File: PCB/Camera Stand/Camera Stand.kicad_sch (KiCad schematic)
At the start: 6 parts, among them J2 HMC5883L, J3 Motor Drive, J4 Keypad 4x4, J9 GPS Module, M5 Motor_Servo, U1 NRF24L01

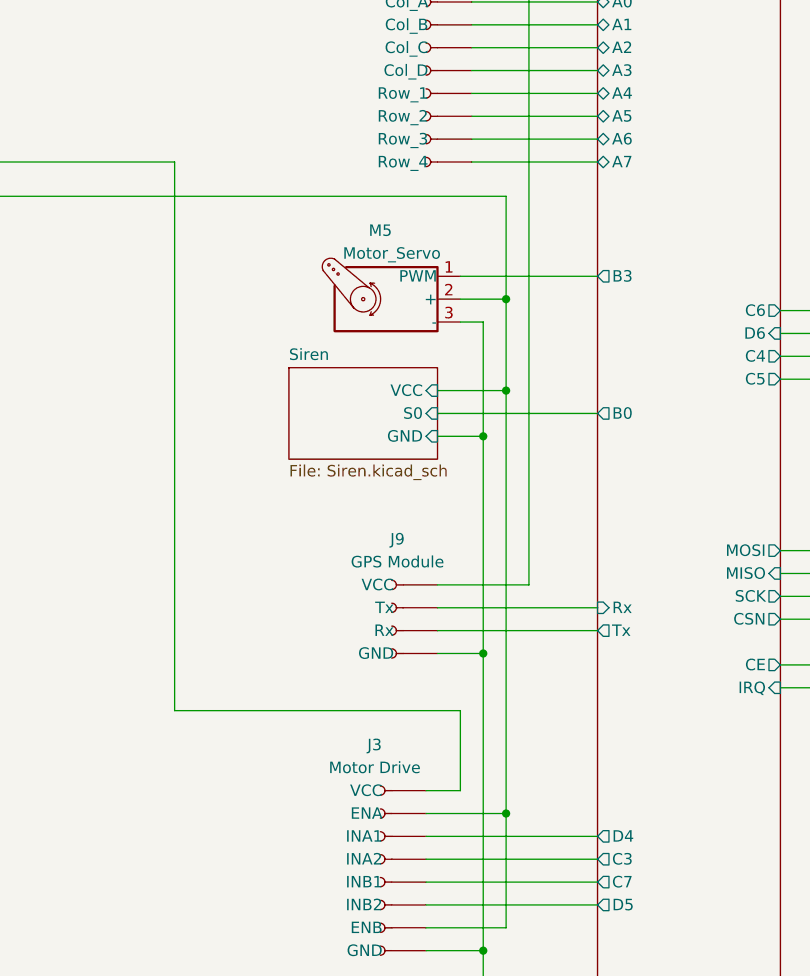
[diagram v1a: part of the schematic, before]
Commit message: 12v to siren
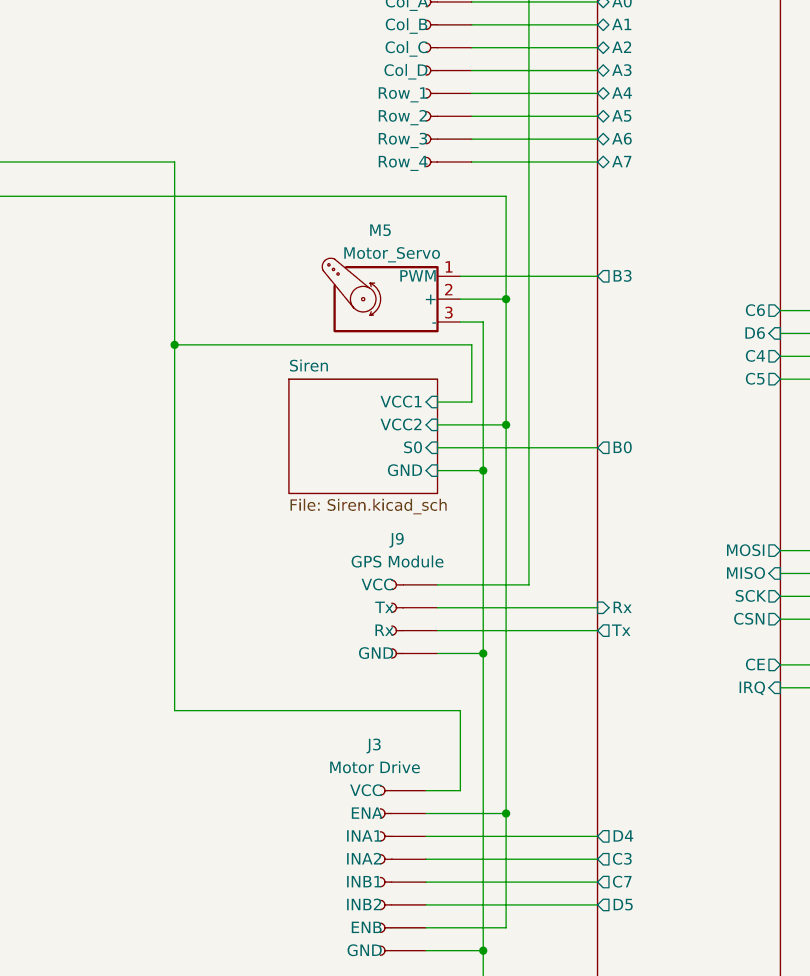
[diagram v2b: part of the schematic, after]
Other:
- sheet Siren ports: added VCC1, VCC2; removed VCC
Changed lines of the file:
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@@
 (kicad_sch (version 20211123) (generator eeschema)
   (paper "A4")
-  (junction (at 146.05 82.55) (diameter 0) (color 0 0 0 0)
-  )
   (junction (at 208.28 59.69) (diameter 0) (color 0 0 0 0)
   )
+  (junction (at 109.22 77.47) (diameter 0) (color 0 0 0 0)
+  )
   (junction (at 148.59 19.05) (diameter 0) (color 0 0 0 0)
   )
@@
   (junction (at 143.51 148.59) (diameter 0) (color 0 0 0 0)
   )
+  (junction (at 143.51 91.44) (diameter 0) (color 0 0 0 0)
+  )
+  (junction (at 146.05 86.36) (diameter 0) (color 0 0 0 0)
+  )
   (junction (at 210.82 29.21) (diameter 0) (color 0 0 0 0)
   )
@@
   (junction (at 146.05 72.39) (diameter 0) (color 0 0 0 0)
   )
-  (junction (at 143.51 87.63) (diameter 0) (color 0 0 0 0)
-  )
   (junction (at 87.63 60.96) (diameter 0) (color 0 0 0 0)
   )
@@
     (stroke (width 0) (type default) (color 0 0 0 0))
   )
+  (wire (pts (xy 138.43 83.82) (xy 142.24 83.82))
+    (stroke (width 0) (type default) (color 0 0 0 0))
+  )
   (wire (pts (xy 176.53 115.57) (xy 217.17 115.57))
     (stroke (width 0) (type default) (color 0 0 0 0))
@@
     (stroke (width 0) (type default) (color 0 0 0 0))
   )
-  (wire (pts (xy 138.43 85.09) (xy 156.21 85.09))
+  (wire (pts (xy 138.43 88.9) (xy 156.21 88.9))
     (stroke (width 0) (type default) (color 0 0 0 0))
   )
@@
     (stroke (width 0) (type default) (color 0 0 0 0))
   )
+  (wire (pts (xy 146.05 72.39) (xy 146.05 86.36))
+    (stroke (width 0) (type default) (color 0 0 0 0))
+  )
   (wire (pts (xy 218.44 71.12) (xy 210.82 71.12))
     (stroke (width 0) (type default) (color 0 0 0 0))
@@
     (stroke (width 0) (type default) (color 0 0 0 0))
   )
-  (wire (pts (xy 143.51 87.63) (xy 143.51 111.76))
-    (stroke (width 0) (type default) (color 0 0 0 0))
-  )
-  (wire (pts (xy 146.05 82.55) (xy 146.05 129.54))
-    (stroke (width 0) (type default) (color 0 0 0 0))
-  )
   (wire (pts (xy 176.53 78.74) (xy 218.44 78.74))
     (stroke (width 0) (type default) (color 0 0 0 0))
@@
     (stroke (width 0) (type default) (color 0 0 0 0))
   )
+  (wire (pts (xy 143.51 91.44) (xy 143.51 111.76))
+    (stroke (width 0) (type default) (color 0 0 0 0))
+  )
   (wire (pts (xy 87.63 148.59) (xy 87.63 156.21))
     (stroke (width 0) (type default) (color 0 0 0 0))
   )
+  (wire (pts (xy 146.05 86.36) (xy 146.05 129.54))
+    (stroke (width 0) (type default) (color 0 0 0 0))
+  )
   (wire (pts (xy 208.28 83.82) (xy 218.44 83.82))
     (stroke (width 0) (type default) (color 0 0 0 0))
@@
     (stroke (width 0) (type default) (color 0 0 0 0))
   )
-  (wire (pts (xy 143.51 74.93) (xy 143.51 87.63))
-    (stroke (width 0) (type default) (color 0 0 0 0))
-  )
   (wire (pts (xy 76.2 60.96) (xy 87.63 60.96))
     (stroke (width 0) (type default) (color 0 0 0 0))
@@
     (stroke (width 0) (type default) (color 0 0 0 0))
   )
-  (wire (pts (xy 146.05 72.39) (xy 146.05 82.55))
-    (stroke (width 0) (type default) (color 0 0 0 0))
-  )
   (wire (pts (xy 143.51 148.59) (xy 156.21 148.59))
     (stroke (width 0) (type default) (color 0 0 0 0))
@@
     (stroke (width 0) (type default) (color 0 0 0 0))
   )
+  (wire (pts (xy 109.22 77.47) (xy 142.24 77.47))
+    (stroke (width 0) (type default) (color 0 0 0 0))
+  )
   (wire (pts (xy 138.43 104.14) (xy 148.59 104.14))
     (stroke (width 0) (type default) (color 0 0 0 0))
   )
+  (wire (pts (xy 143.51 74.93) (xy 143.51 91.44))
+    (stroke (width 0) (type default) (color 0 0 0 0))
+  )
   (wire (pts (xy 76.2 57.15) (xy 109.22 57.15))
     (stroke (width 0) (type default) (color 0 0 0 0))
   )
+  (wire (pts (xy 109.22 77.47) (xy 109.22 118.11))
+    (stroke (width 0) (type default) (color 0 0 0 0))
+  )
   (wire (pts (xy 218.44 52.07) (xy 205.74 52.07))
     (stroke (width 0) (type default) (color 0 0 0 0))
@@
     (stroke (width 0) (type default) (color 0 0 0 0))
   )
+  (wire (pts (xy 142.24 83.82) (xy 142.24 77.47))
+    (stroke (width 0) (type default) (color 0 0 0 0))
+  )
   (wire (pts (xy 85.09 19.05) (xy 148.59 19.05))
     (stroke (width 0) (type default) (color 0 0 0 0))
@@
     (stroke (width 0) (type default) (color 0 0 0 0))
   )
-  (wire (pts (xy 109.22 57.15) (xy 109.22 118.11))
+  (wire (pts (xy 109.22 57.15) (xy 109.22 77.47))
     (stroke (width 0) (type default) (color 0 0 0 0))
   )
@@
     (stroke (width 0) (type default) (color 0 0 0 0))
   )
-  (wire (pts (xy 143.51 87.63) (xy 138.43 87.63))
+  (wire (pts (xy 143.51 91.44) (xy 138.43 91.44))
     (stroke (width 0) (type default) (color 0 0 0 0))
   )
@@
     (stroke (width 0) (type default) (color 0 0 0 0))
   )
-  (wire (pts (xy 146.05 82.55) (xy 138.43 82.55))
+  (wire (pts (xy 146.05 86.36) (xy 138.43 86.36))
     (stroke (width 0) (type default) (color 0 0 0 0))
   )
@@
     )
   )
-  (sheet (at 121.92 80.01) (size 16.51 10.16) (fields_autoplaced)
+  (sheet (at 121.92 81.28) (size 16.51 12.7) (fields_autoplaced)
     (stroke (width 0.1524) (type solid) (color 0 0 0 0))
     (fill (color 0 0 0 0.0000))
-    (property "Sheet name" "Siren" (id 0) (at 121.92 79.2984 0)
+    (property "Sheet name" "Siren" (id 0) (at 121.92 80.5684 0)
       (effects (font (size 1.27 1.27)) (justify left bottom))
     )
-    (property "Sheet file" "Siren.kicad_sch" (id 1) (at 121.92 90.7546 0)
+    (property "Sheet file" "Siren.kicad_sch" (id 1) (at 121.92 94.5646 0)
       (effects (font (size 1.27 1.27)) (justify left top))
     )
-    (pin "S0" input (at 138.43 85.09 0)
-      (effects (font (size 1.27 1.27)) (justify right))
-    )
-    (pin "GND" input (at 138.43 87.63 0)
-      (effects (font (size 1.27 1.27)) (justify right))
-    )
-    (pin "VCC" input (at 138.43 82.55 0)
+    (pin "S0" input (at 138.43 88.9 0)
+      (effects (font (size 1.27 1.27)) (justify right))
+    )
+    (pin "GND" input (at 138.43 91.44 0)
+      (effects (font (size 1.27 1.27)) (justify right))
+    )
+    (pin "VCC1" input (at 138.43 83.82 0)
+      (effects (font (size 1.27 1.27)) (justify right))
+    )
+    (pin "VCC2" input (at 138.43 86.36 0)
       (effects (font (size 1.27 1.27)) (justify right))
     )
@@
       (effects (font (size 1.27 1.27)) (justify right))
     )
-    (pin "B0" output (at 156.21 85.09 180)
-      (effects (font (size 1.27 1.27)) (justify left))
-    )
+    (pin "B0" output (at 156.21 88.9 180)
+      (effects (font (size 1.27 1.27)) (justify left))
+    )
